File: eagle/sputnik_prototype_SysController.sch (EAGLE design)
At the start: 66 parts, among them U1 MEGA128-A

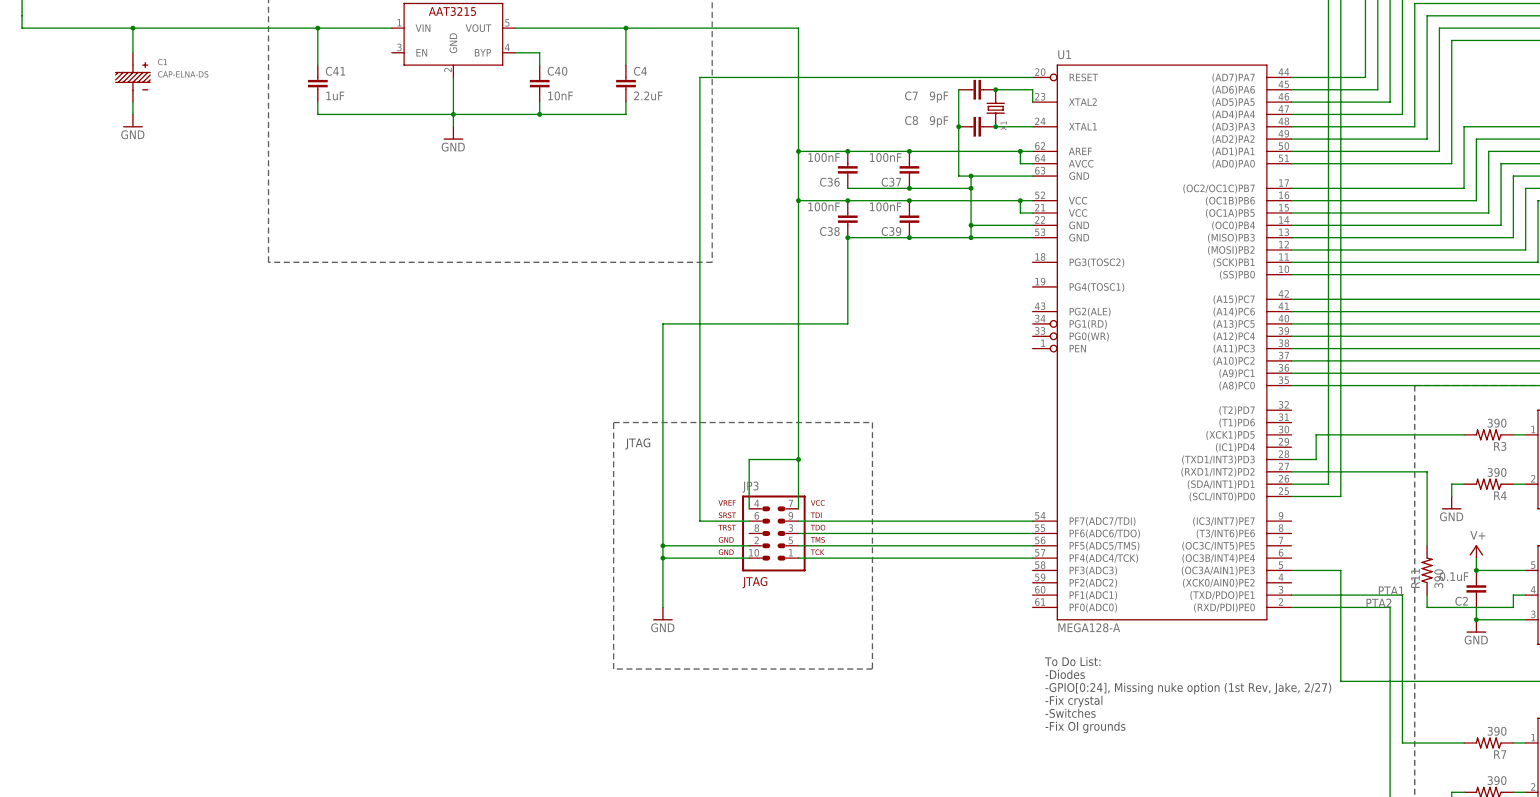
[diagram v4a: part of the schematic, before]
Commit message: Added the diodes and fixed the Crystal
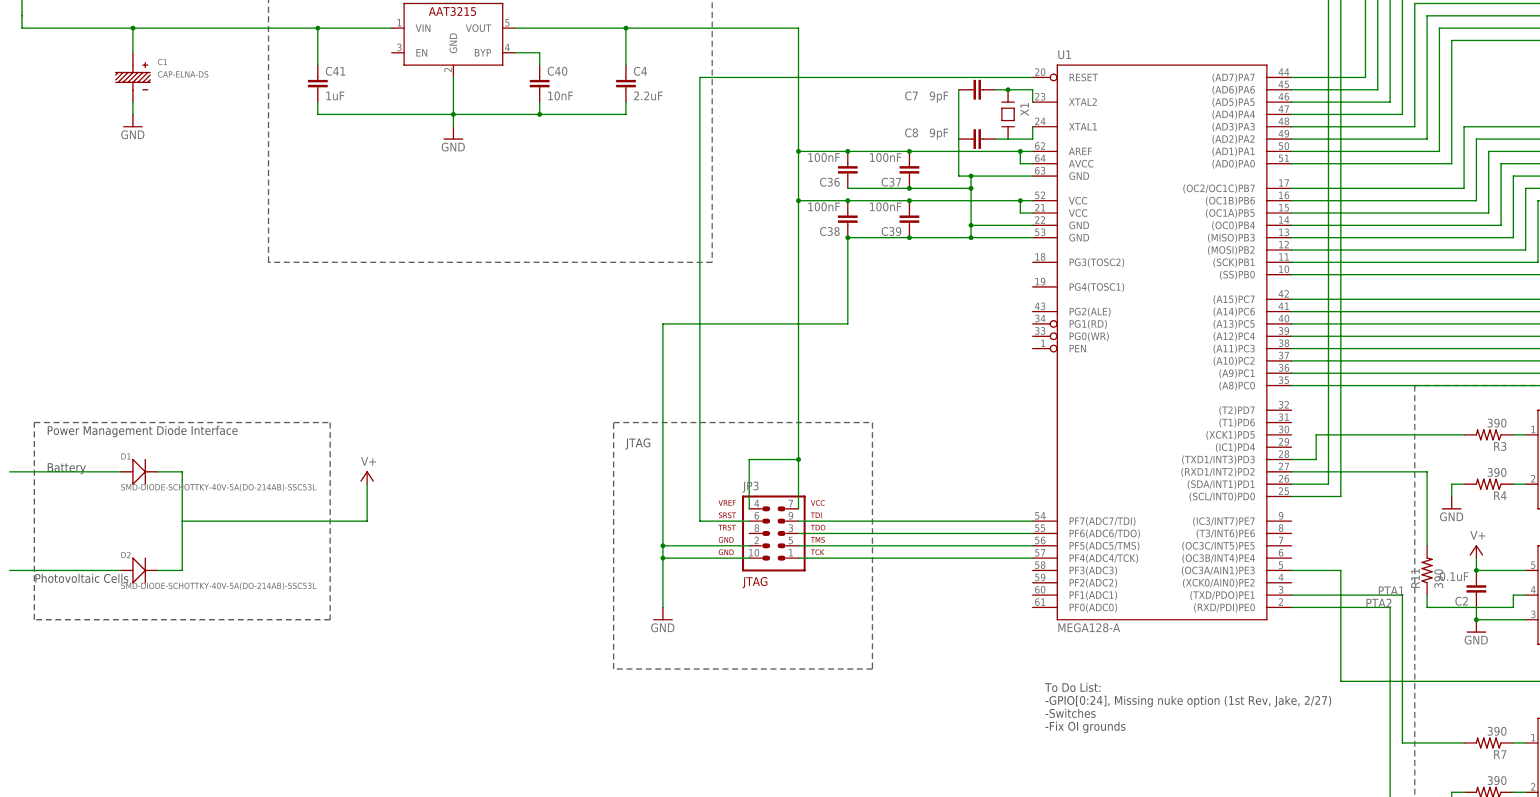
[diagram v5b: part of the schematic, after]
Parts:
- added D1, D2: SMD-DIODE-SCHOTTKY-40V-5A(DO-214AB)-SSC53L, SMD-DIODE-SCHOTTKY-40V-5A_DO-214AB_ SSC53L:SMD-DIODE-SCHOTTKY-40V-5A(DO-214AB)-SSC53L
- X1: value (none) -> CRYSTAL-ABRACON-ABM3-SMD; device monitor-v2:CRYSTAL-3.2X1.5-A -> crystal-abracon-abm3-smd:CRYSTAL-ABRACON-ABM3-SMD; DIST Digi-Key -> (none); DPN 535-10630-1-ND -> (none); MFN Abracon LLC -> (none); MPN ABM3-8.00MHZ-D2Y-T -> (none)
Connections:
- removed net N$22: C8.2, U1.XTAL1, X1.2
- new net N$1: C8.2, U1.XTAL1, X1.P$2
- new net N$25: D1.+
- new net N$26: D2.+
- net N$17: now also X1.P$1; no longer X1.1
- net V+: now also D1.-, D2.-
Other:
- note added: "Battery"
- note added: "Photovoltaic Cells"
- note added: "Power Management Diode Interface"
- note added: "To Do List: -GPIO[0:24], Missing nuke option (1st Rev, Jake, 2/27) -Switches -Fix OI grounds"
- note removed: "To Do List: -Diodes -GPIO[0:24], Missing nuke option (1st Rev, Jake, 2/27) -Fix crystal -Switches -Fix OI grounds"
- moved on the sheet: C8
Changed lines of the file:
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@@
 <?xml version="1.0" encoding="utf-8"?>
 <!DOCTYPE eagle SYSTEM "eagle.dtd">
-<eagle version="7.5.0">
+<eagle version="7.4.0">
 <drawing>
 <settings>
@@
 <setting verticaltext="up"/>
 </settings>
-<grid distance="0.1" unitdist="inch" unit="inch" style="lines" multiple="1" display="no" altdistance="0.01" altunitdist="inch" altunit="inch"/>
+<grid distance="0.1" unitdist="inch" unit="inch" style="lines" multiple="1" display="yes" altdistance="0.01" altunitdist="inch" altunit="inch"/>
 <layers>
 <layer number="1" name="Top" color="4" fill="1" visible="no" active="no"/>
@@
 <part name="GND16" library="psas_c3_team05" deviceset="GND" device=""/>
 <part name="C6" library="rcl_custom" deviceset="C-EU" device="0603-B-NOSILK" value="0.1uF"/>
-<part name="X1" library="monitor-v2" deviceset="CRYSTAL" device="-3.2X1.5-A">
-<attribute name="DIST" value="Digi-Key"/>
-<attribute name="DPN" value="535-10630-1-ND"/>
-<attribute name="MFN" value="Abracon LLC"/>
-<attribute name="MPN" value="ABM3-8.00MHZ-D2Y-T"/>
-</part>
 <part name="C7" library="rcl_custom" deviceset="C-EU" device="0603-B-NOSILK" value="9pF"/>
 <part name="C8" library="rcl_custom" deviceset="C-EU" device="0603-B-NOSILK" value="9pF"/>
@@
 <part name="C40" library="rcl_custom" deviceset="C-EU" device="0402-B-NOSILK" value="10nF"/>
 <part name="C41" library="rcl_custom" deviceset="C-EU" device="0402-B-NOSILK" value="1uF"/>
+<part name="D1" library="SMD-DIODE-SCHOTTKY-40V-5A_DO-214AB_ SSC53L" deviceset="SMD-DIODE-SCHOTTKY-40V-5A(DO-214AB)-SSC53L" device=""/>
+<part name="D2" library="SMD-DIODE-SCHOTTKY-40V-5A_DO-214AB_ SSC53L" deviceset="SMD-DIODE-SCHOTTKY-40V-5A(DO-214AB)-SSC53L" device=""/>
+<part name="SUPPLY9" library="psas_c3_team05" deviceset="V+" device=""/>
+<part name="X1" library="crystal-abracon-abm3-smd" deviceset="CRYSTAL-ABRACON-ABM3-SMD" device=""/>
 </parts>
 <sheets>
@@
 <text x="429.26" y="154.94" size="1.778" layer="97">Low-gain Radio (KW0x)</text>
 <text x="284.48" y="134.62" size="1.778" layer="97">To Do List:
--Diodes
 -GPIO[0:24], Missing nuke option (1st Rev, Jake, 2/27)
--Fix crystal
 -Switches
 -Fix OI grounds</text>
@@
 <text x="370.84" y="101.6" size="1.778" layer="97">Optocouplers</text>
 <text x="137.16" y="297.18" size="1.778" layer="97">TODO: Replace this. We need a part that has a rad-hard analogue</text>
+<wire x1="76.2" y1="198.12" x2="137.16" y2="198.12" width="0.1524" layer="97" style="longdash"/>
+<wire x1="137.16" y1="198.12" x2="137.16" y2="157.48" width="0.1524" layer="97" style="longdash"/>
+<wire x1="137.16" y1="157.48" x2="76.2" y2="157.48" width="0.1524" layer="97" style="longdash"/>
+<wire x1="76.2" y1="157.48" x2="76.2" y2="198.12" width="0.1524" layer="97" style="longdash"/>
+<text x="78.74" y="195.58" size="1.778" layer="97">Power Management Diode Interface</text>
+<text x="78.74" y="187.96" size="1.778" layer="97">Battery</text>
+<text x="76.2" y="165.1" size="1.778" layer="97">Photovoltaic Cells</text>
 </plain>
 <instances>
@@
 <instance part="GND16" gate="1" x="419.1" y="119.38"/>
 <instance part="C6" gate="CE" x="419.1" y="127" rot="R180"/>
-<instance part="X1" gate="X" x="274.32" y="261.62" rot="R270">
-<attribute name="MFN" x="274.32" y="261.62" size="1.778" layer="96" rot="R270" display="off"/>
-<attribute name="MPN" x="274.32" y="261.62" size="1.778" layer="96" rot="R270" display="off"/>
-<attribute name="DIST" x="274.32" y="261.62" size="1.778" layer="96" rot="R270" display="off"/>
-<attribute name="DPN" x="274.32" y="261.62" size="1.778" layer="96" rot="R270" display="off"/>
-</instance>
 <instance part="C7" gate="CE" x="269.24" y="266.7" smashed="yes" rot="R90">
 <attribute name="NAME" x="255.524" y="264.541" size="1.778" layer="95"/>
 <attribute name="VALUE" x="260.604" y="264.541" size="1.778" layer="96"/>
 </instance>
-<instance part="C8" gate="CE" x="269.24" y="259.08" smashed="yes" rot="R90">
-<attribute name="NAME" x="255.524" y="259.461" size="1.778" layer="95"/>
-<attribute name="VALUE" x="260.604" y="259.461" size="1.778" layer="96"/>
+<instance part="C8" gate="CE" x="269.24" y="256.54" smashed="yes" rot="R90">
+<attribute name="NAME" x="255.524" y="256.921" size="1.778" layer="95"/>
+<attribute name="VALUE" x="260.604" y="256.921" size="1.778" layer="96"/>
 </instance>
 <instance part="GND8" gate="1" x="368.3" y="180.34"/>
@@
 <instance part="C40" gate="CE" x="180.34" y="269.24"/>
 <instance part="C41" gate="CE" x="134.62" y="269.24"/>
+<instance part="D1" gate="G$1" x="97.79" y="187.96"/>
+<instance part="D2" gate="G$1" x="97.79" y="167.64"/>
+<instance part="SUPPLY9" gate="1" x="144.78" y="187.96"/>
+<instance part="X1" gate="G$1" x="276.86" y="261.62" rot="R270"/>
 </instances>
 <busses>
@@
 <wire x1="243.84" y1="218.44" x2="243.84" y2="236.22" width="0.1524" layer="91"/>
 <junction x="243.84" y="236.22"/>
-<pinref part="C7" gate="CE" pin="1"/>
 <pinref part="C8" gate="CE" pin="1"/>
-<wire x1="266.7" y1="259.08" x2="266.7" y2="266.7" width="0.1524" layer="91"/>
-<wire x1="266.7" y1="259.08" x2="266.7" y2="248.92" width="0.1524" layer="91"/>
-<junction x="266.7" y="259.08"/>
+<wire x1="266.7" y1="256.54" x2="266.7" y2="248.92" width="0.1524" layer="91"/>
 <wire x1="266.7" y1="248.92" x2="269.24" y2="248.92" width="0.1524" layer="91"/>
 <junction x="269.24" y="248.92"/>
+<pinref part="C7" gate="CE" pin="1"/>
+<wire x1="266.7" y1="266.7" x2="266.7" y2="256.54" width="0.1524" layer="91"/>
 </segment>
 <segment>
@@
 <pinref part="U$4" gate="G$1" pin="VDD"/>
 </segment>
+<segment>
+<pinref part="D1" gate="G$1" pin="-"/>
+<wire x1="101.6" y1="187.96" x2="106.68" y2="187.96" width="0.1524" layer="91"/>
+<wire x1="106.68" y1="187.96" x2="106.68" y2="177.8" width="0.1524" layer="91"/>
+<pinref part="D2" gate="G$1" pin="-"/>
+<wire x1="106.68" y1="177.8" x2="106.68" y2="167.64" width="0.1524" layer="91"/>
+<wire x1="106.68" y1="167.64" x2="101.6" y2="167.64" width="0.1524" layer="91"/>
+<wire x1="106.68" y1="177.8" x2="144.78" y2="177.8" width="0.1524" layer="91"/>
+<wire x1="144.78" y1="177.8" x2="144.78" y2="185.42" width="0.1524" layer="91"/>
+<pinref part="SUPPLY9" gate="1" pin="V+"/>
+</segment>
 </net>
 <net name="SDL" class="0">
@@
 <net name="N$17" class="0">
 <segment>
-<pinref part="X1" gate="X" pin="1"/>
 <pinref part="C7" gate="CE" pin="2"/>
 <pinref part="U1" gate="G$1" pin="XTAL2"/>
-<wire x1="274.32" y1="266.7" x2="281.94" y2="266.7" width="0.1524" layer="91"/>
+<wire x1="274.32" y1="266.7" x2="276.86" y2="266.7" width="0.1524" layer="91"/>
+<wire x1="276.86" y1="266.7" x2="281.94" y2="266.7" width="0.1524" layer="91"/>
 <wire x1="281.94" y1="266.7" x2="281.94" y2="264.16" width="0.1524" layer="91"/>
-<junction x="274.32" y="266.7"/>
-</segment>
-</net>
-<net name="N$22" class="0">
-<segment>
-<pinref part="X1" gate="X" pin="2"/>
-<pinref part="C8" gate="CE" pin="2"/>
-<pinref part="U1" gate="G$1" pin="XTAL1"/>
-<wire x1="274.32" y1="259.08" x2="281.94" y2="259.08" width="0.1524" layer="91"/>
-<junction x="274.32" y="259.08"/>
+<pinref part="X1" gate="G$1" pin="P$1"/>
+<junction x="276.86" y="266.7"/>
 </segment>
 </net>
@@
 </segment>
 </net>
+<net name="N$25" class="0">
+<segment>
+<pinref part="D1" gate="G$1" pin="+"/>
+<wire x1="93.98" y1="187.96" x2="71.12" y2="187.96" width="0.1524" layer="91"/>
+</segment>
+</net>
+<net name="N$26" class="0">
+<segment>
+<pinref part="D2" gate="G$1" pin="+"/>
+<wire x1="93.98" y1="167.64" x2="71.12" y2="167.64" width="0.1524" layer="91"/>
+</segment>
+</net>
+<net name="N$1" class="0">
+<segment>
+<pinref part="C8" gate="CE" pin="2"/>
+<pinref part="X1" gate="G$1" pin="P$2"/>
+<wire x1="274.32" y1="256.54" x2="276.86" y2="256.54" width="0.1524" layer="91"/>
+<wire x1="276.86" y1="256.54" x2="281.94" y2="256.54" width="0.1524" layer="91"/>
+<pinref part="U1" gate="G$1" pin="XTAL1"/>
+<wire x1="281.94" y1="259.08" x2="281.94" y2="256.54" width="0.1524" layer="91"/>
+</segment>
+</net>
